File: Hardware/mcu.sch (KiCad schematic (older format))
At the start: 10 parts, among them SW3 SW_PUSH, U1 STM32F411RE_LQFP64

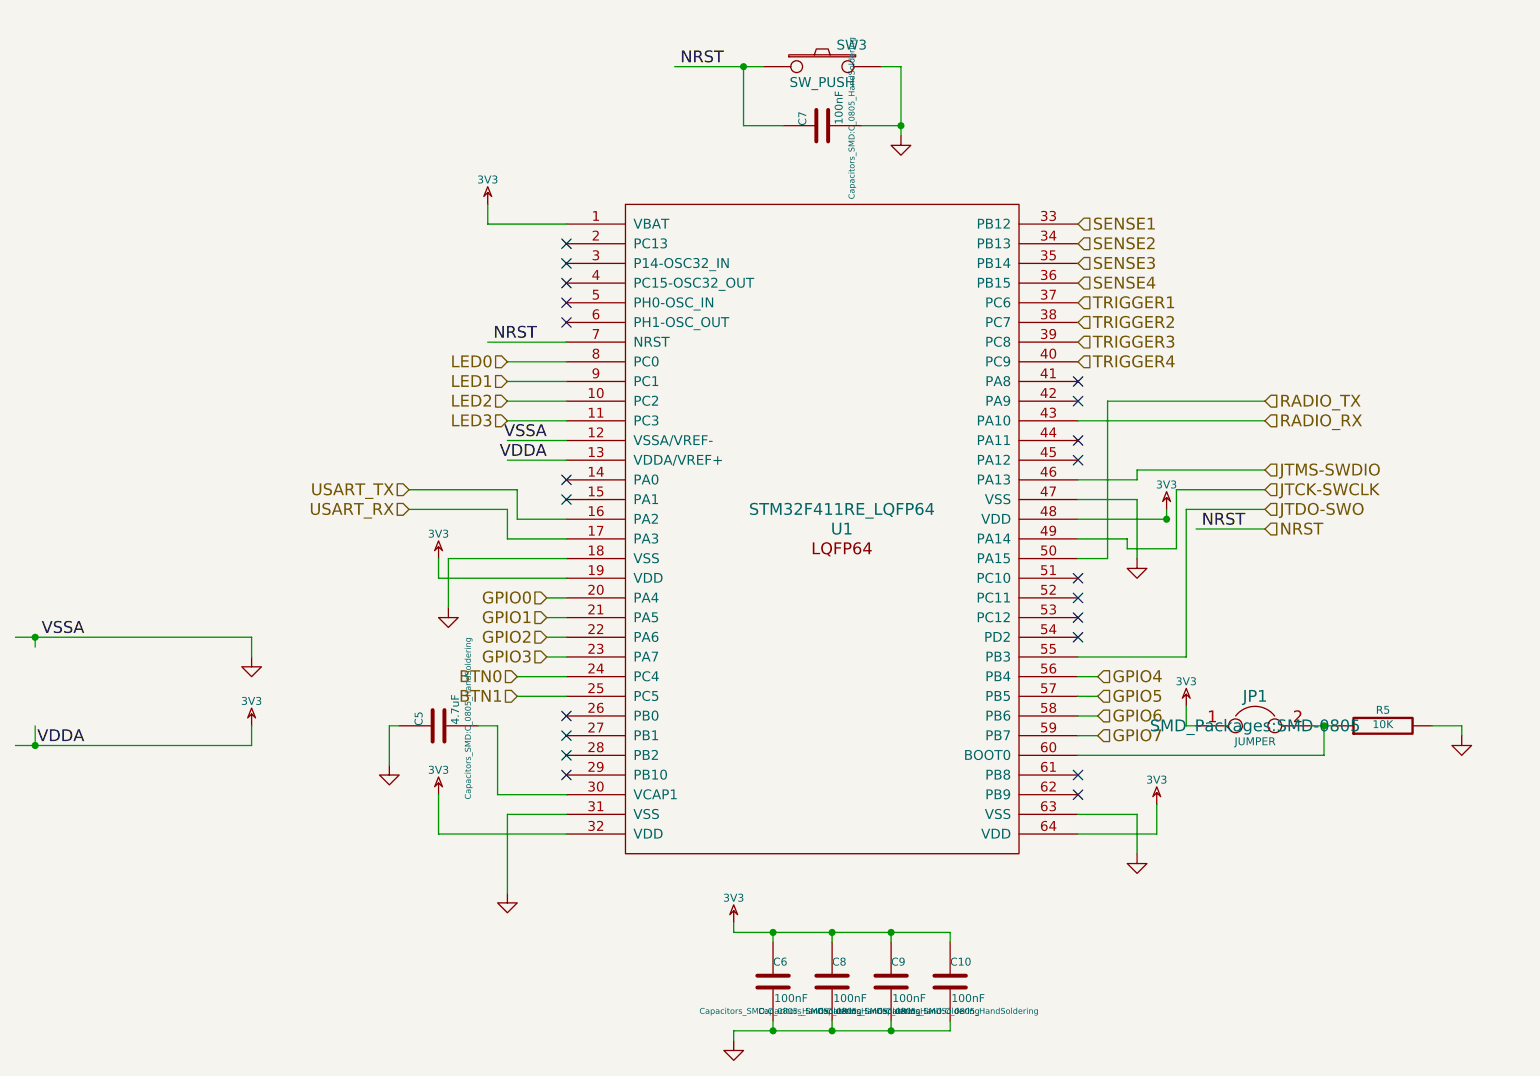
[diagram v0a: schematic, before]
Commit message: Added sensors and sensor passives
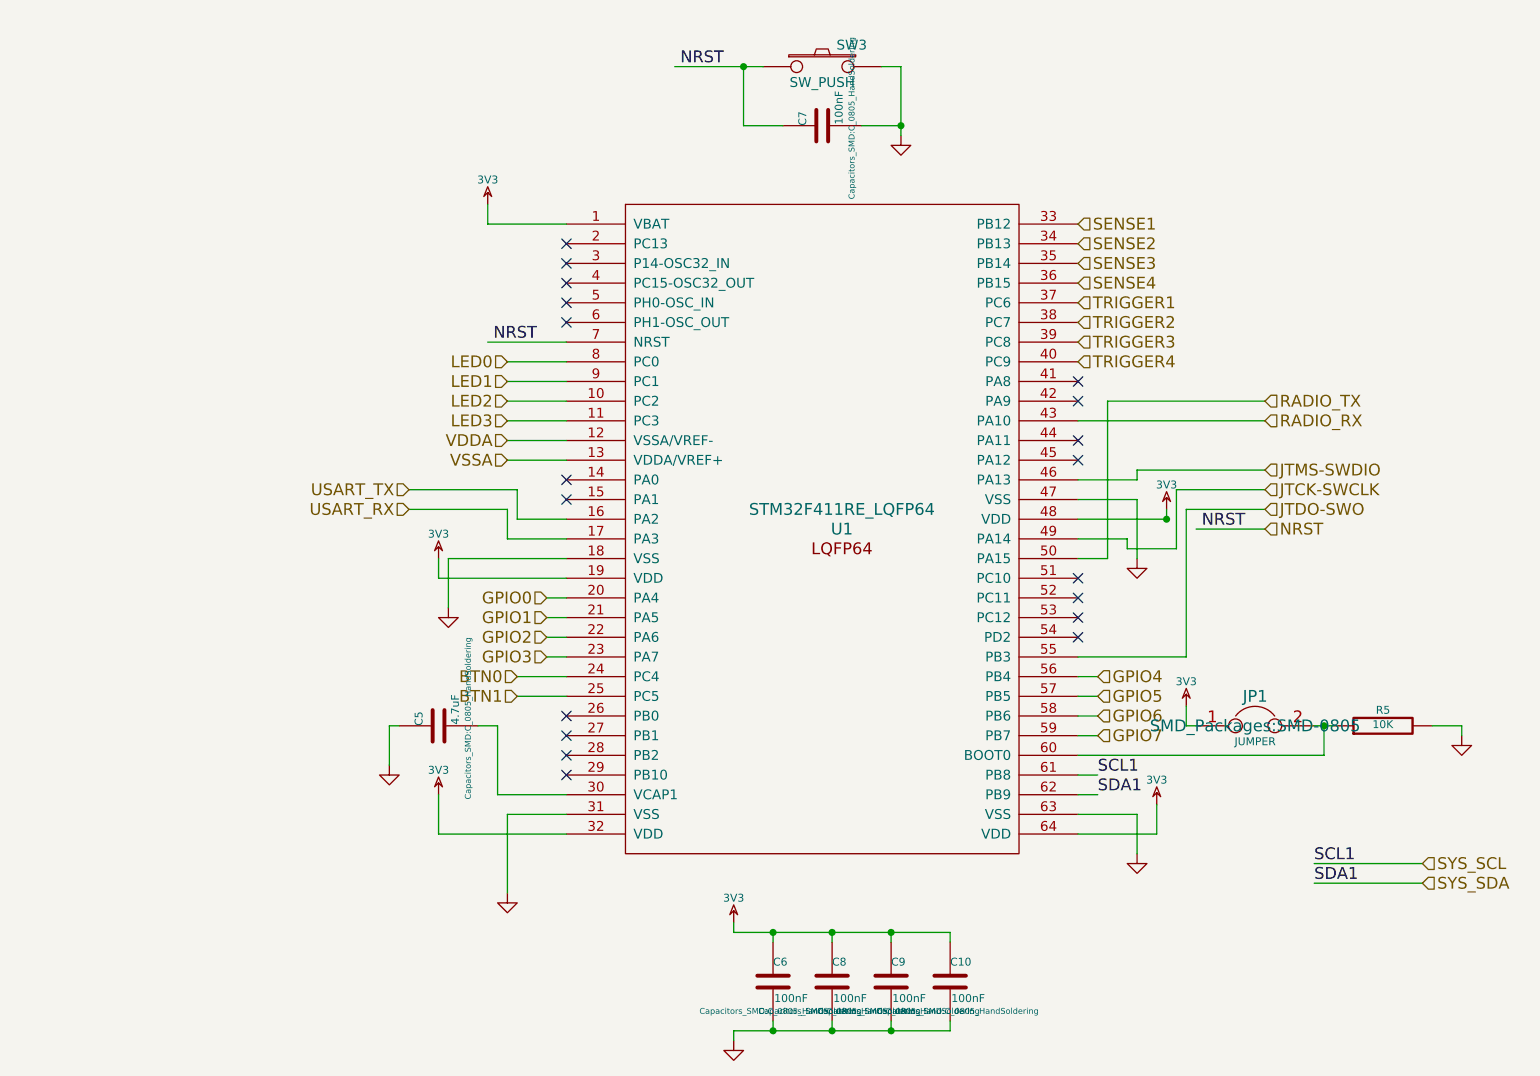
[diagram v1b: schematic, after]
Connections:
- net labels added: SCL1, SDA1, SYS_SCL, SYS_SDA
- wire segments 93 -> 91
- no-connect marks 21 -> 19
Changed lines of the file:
@@
 LIBS:STM32-Additional
 LIBS:xbee
+LIBS:Passives
 LIBS:avbay-cache
-EELAYER 27 0
+EELAYER 25 0
 EELAYER END
 $Descr USLetter 11000 8500
 encoding utf-8
-Sheet 2 4
+Sheet 4 5
 Title "MCU"
 Date "6 dec 2014"
@@
 $EndDescr
 $Comp
-L 3V3 #PWR12
+L 3V3 #PWR018
 U 1 1 542CDA8F
 P 3800 3600
-F 0 "#PWR12" H 3800 3700 40  0001 C CNN
+F 0 "#PWR018" H 3800 3700 40  0001 C CNN
 F 1 "3V3" H 3800 3725 40  0000 C CNN
 F 2 "" H 3800 3600 60  0000 C CNN
@@
 $EndComp
 $Comp
-L GND #PWR14
+L GND #PWR019
 U 1 1 542CDA9E
 P 3850 3850
-F 0 "#PWR14" H 3850 3850 30  0001 C CNN
+F 0 "#PWR019" H 3850 3850 30  0001 C CNN
 F 1 "GND" H 3850 3780 30  0001 C CNN
 F 2 "" H 3850 3850 60  0000 C CNN
@@
 $EndComp
 $Comp
-L 3V3 #PWR13
+L 3V3 #PWR020
 U 1 1 542CDAB1
 P 3800 4800
-F 0 "#PWR13" H 3800 4900 40  0001 C CNN
+F 0 "#PWR020" H 3800 4900 40  0001 C CNN
 F 1 "3V3" H 3800 4925 40  0000 C CNN
 F 2 "" H 3800 4800 60  0000 C CNN
@@
 $EndComp
 $Comp
-L 3V3 #PWR22
+L 3V3 #PWR021
 U 1 1 542CDAB7
 P 7450 4850
-F 0 "#PWR22" H 7450 4950 40  0001 C CNN
+F 0 "#PWR021" H 7450 4950 40  0001 C CNN
 F 1 "3V3" H 7450 4975 40  0000 C CNN
 F 2 "" H 7450 4850 60  0000 C CNN
@@
 $EndComp
 $Comp
-L 3V3 #PWR23
+L 3V3 #PWR022
 U 1 1 542CDC4D
 P 7500 3350
-F 0 "#PWR23" H 7500 3450 40  0001 C CNN
+F 0 "#PWR022" H 7500 3450 40  0001 C CNN
 F 1 "3V3" H 7500 3475 40  0000 C CNN
 F 2 "" H 7500 3350 60  0000 C CNN
@@
 $EndComp
 $Comp
-L GND #PWR19
+L GND #PWR023
 U 1 1 5430D873
 P 6150 1450
-F 0 "#PWR19" H 6150 1450 30  0001 C CNN
+F 0 "#PWR023" H 6150 1450 30  0001 C CNN
 F 1 "GND" H 6150 1380 30  0001 C CNN
 F 2 "" H 6150 1450 60  0000 C CNN
@@
 $EndComp
 $Comp
-L 3V3 #PWR24
+L 3V3 #PWR024
 U 1 1 5430DC01
 P 7600 4350
-F 0 "#PWR24" H 7600 4450 40  0001 C CNN
+F 0 "#PWR024" H 7600 4450 40  0001 C CNN
 F 1 "3V3" H 7600 4475 40  0000 C CNN
 F 2 "" H 7600 4350 60  0000 C CNN
@@
 $EndComp
 $Comp
-L GND #PWR25
+L GND #PWR025
 U 1 1 5430DC07
 P 9000 4500
-F 0 "#PWR25" H 9000 4500 30  0001 C CNN
+F 0 "#PWR025" H 9000 4500 30  0001 C CNN
 F 1 "GND" H 9000 4430 30  0001 C CNN
 F 2 "" H 9000 4500 60  0000 C CNN
@@
 $EndComp
 $Comp
-L 3V3 #PWR17
+L 3V3 #PWR026
 U 1 1 5430E0CC
 P 5300 5450
-F 0 "#PWR17" H 5300 5550 40  0001 C CNN
+F 0 "#PWR026" H 5300 5550 40  0001 C CNN
 F 1 "3V3" H 5300 5575 40  0000 C CNN
 F 2 "" H 5300 5450 60  0000 C CNN
@@
 $EndComp
 $Comp
-L GND #PWR18
+L GND #PWR027
 U 1 1 5430E365
 P 5300 6050
-F 0 "#PWR18" H 5300 6050 30  0001 C CNN
+F 0 "#PWR027" H 5300 6050 30  0001 C CNN
 F 1 "GND" H 5300 5980 30  0001 C CNN
 F 2 "" H 5300 6050 60  0000 C CNN
@@
 $EndComp
 $Comp
-L GND #PWR11
+L GND #PWR028
 U 1 1 5430E5BA
 P 3550 4650
-F 0 "#PWR11" H 3550 4650 30  0001 C CNN
+F 0 "#PWR028" H 3550 4650 30  0001 C CNN
 F 1 "GND" H 3550 4580 30  0001 C CNN
 F 2 "" H 3550 4650 60  0000 C CNN
@@
 Text HLabel 8000 2900 2    60   Input ~ 0
 RADIO_RX
-Text Label 4350 3100 2    60   ~ 0
-VDDA
-Text Label 4350 3000 2    60   ~ 0
-VSSA
-Text Label 2000 4000 2    60   ~ 0
-VSSA
-Text Label 2000 4550 2    60   ~ 0
-VDDA
-$Comp
-L 3V3 #PWR15
+$Comp
+L 3V3 #PWR029
 U 1 1 5430E17B
 P 4050 1800
-F 0 "#PWR15" H 4050 1900 40  0001 C CNN
+F 0 "#PWR029" H 4050 1900 40  0001 C CNN
 F 1 "3V3" H 4050 1925 40  0000 C CNN
 F 2 "" H 4050 1800 60  0000 C CNN
 F 3 "" H 4050 1800 60  0000 C CNN
 	1    4050 1800
-	1    0    0    -1
-$EndComp
-$Comp
-L GND #PWR9
-U 1 1 5430E3DA
-P 2850 4100
-F 0 "#PWR9" H 2850 4100 30  0001 C CNN
-F 1 "GND" H 2850 4030 30  0001 C CNN
-F 2 "" H 2850 4100 60  0000 C CNN
-F 3 "" H 2850 4100 60  0000 C CNN
-	1    2850 4100
-	1    0    0    -1
-$EndComp
-$Comp
-L 3V3 #PWR10
-U 1 1 5430E3E0
-P 2850 4450
-F 0 "#PWR10" H 2850 4550 40  0001 C CNN
-F 1 "3V3" H 2850 4575 40  0000 C CNN
-F 2 "" H 2850 4450 60  0000 C CNN
-F 3 "" H 2850 4450 60  0000 C CNN
-	1    2850 4450
 	1    0    0    -1
 $EndComp
@@
 	7200 2800 8000 2800
 Wire Wire Line
-	1650 4000 2850 4000
-Wire Wire Line
-	1650 4550 2850 4550
-Wire Wire Line
 	4050 1900 4450 1900
 Wire Wire Line
 	4050 1800 4050 1900
-Wire Wire Line
-	2850 4000 2850 4100
-Wire Wire Line
-	2850 4550 2850 4450
-Wire Wire Line
-	1750 4450 1750 4550
-Connection ~ 1750 4550
-Wire Wire Line
-	1750 4050 1750 4000
-Connection ~ 1750 4000
 Wire Wire Line
 	8000 2900 7050 2900
@@
 NoConn ~ 7050 3900
 NoConn ~ 7050 4000
-NoConn ~ 7050 4700
-NoConn ~ 7050 4800
 NoConn ~ 4450 4700
 NoConn ~ 4450 4600
@@
 	4150 4900 4150 5300
 $Comp
-L GND #PWR16
+L GND #PWR030
 U 1 1 54449600
 P 4150 5300
-F 0 "#PWR16" H 4150 5300 30  0001 C CNN
+F 0 "#PWR030" H 4150 5300 30  0001 C CNN
 F 1 "GND" H 4150 5230 30  0001 C CNN
 F 2 "" H 4150 5300 60  0000 C CNN
@@
 	7350 4900 7350 5100
 $Comp
-L GND #PWR20
+L GND #PWR031
 U 1 1 5444A762
 P 7350 3600
-F 0 "#PWR20" H 7350 3600 30  0001 C CNN
+F 0 "#PWR031" H 7350 3600 30  0001 C CNN
 F 1 "GND" H 7350 3530 30  0001 C CNN
 F 2 "" H 7350 3600 60  0000 C CNN
@@
 	7350 3300 7350 3600
 $Comp
-L GND #PWR21
+L GND #PWR032
 U 1 1 54449656
 P 7350 5100
-F 0 "#PWR21" H 7350 5100 30  0001 C CNN
+F 0 "#PWR032" H 7350 5100 30  0001 C CNN
 F 1 "GND" H 7350 5030 30  0001 C CNN
 F 2 "" H 7350 5100 60  0000 C CNN
@@
 NoConn ~ 4450 2300
 NoConn ~ 4450 2400
+Wire Wire Line
+	7050 4700 7150 4700
+Wire Wire Line
+	7050 4800 7150 4800
+Text Label 7150 4700 0    60   ~ 0
+SCL1
+Text Label 7150 4800 0    60   ~ 0
+SDA1
+Wire Wire Line
+	8250 5150 8800 5150
+Wire Wire Line
+	8250 5250 8800 5250
+Text Label 8250 5150 0    60   ~ 0
+SCL1
+Text Label 8250 5250 0    60   ~ 0
+SDA1
+Text HLabel 8800 5150 2    60   Input ~ 0
+SYS_SCL
+Text HLabel 8800 5250 2    60   Input ~ 0
+SYS_SDA
+Text HLabel 4150 3000 0    60   Input ~ 0
+VDDA
+Text HLabel 4150 3100 0    60   Input ~ 0
+VSSA
 $EndSCHEMATC

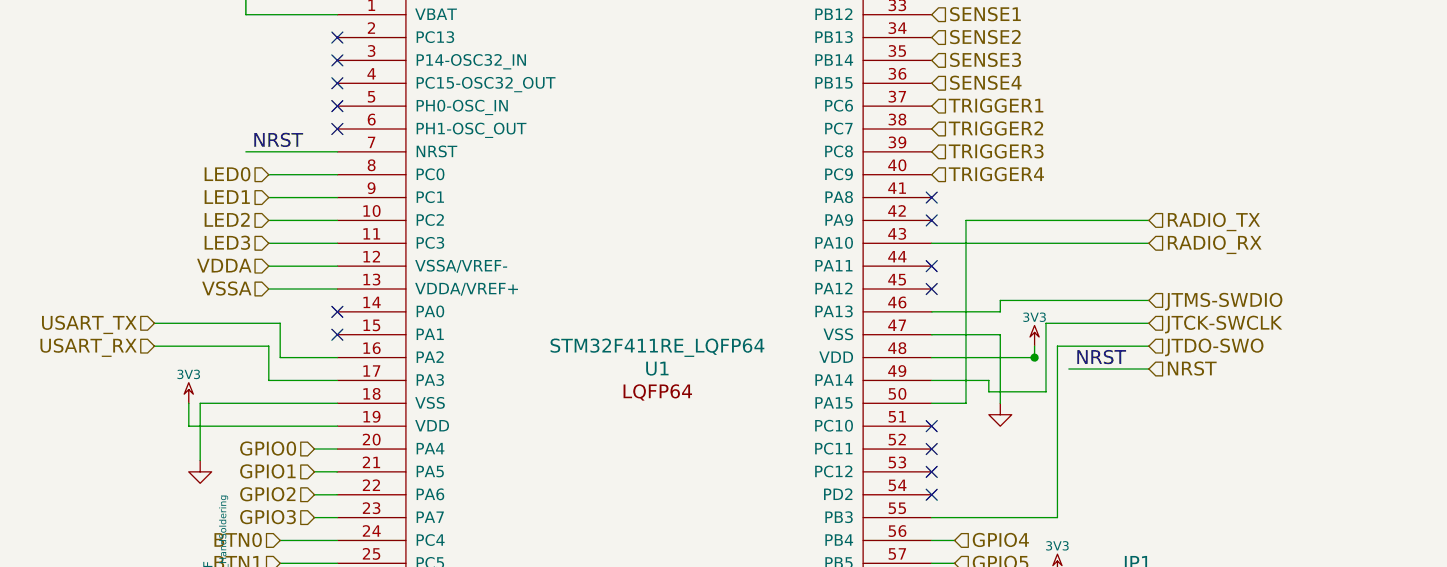
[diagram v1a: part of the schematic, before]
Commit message: Roughed out PCB layout
Known issues:
- SW_PUSH holes too small. New footprint needed
- Sensor footprints are completely wrong.
- Regulator footprints might not be correct.

Tasks:
- Place passives according to schematic (especially
  with decoupling capacitors.
- Condense layout as much as possible for
  smallest board size
- Route board
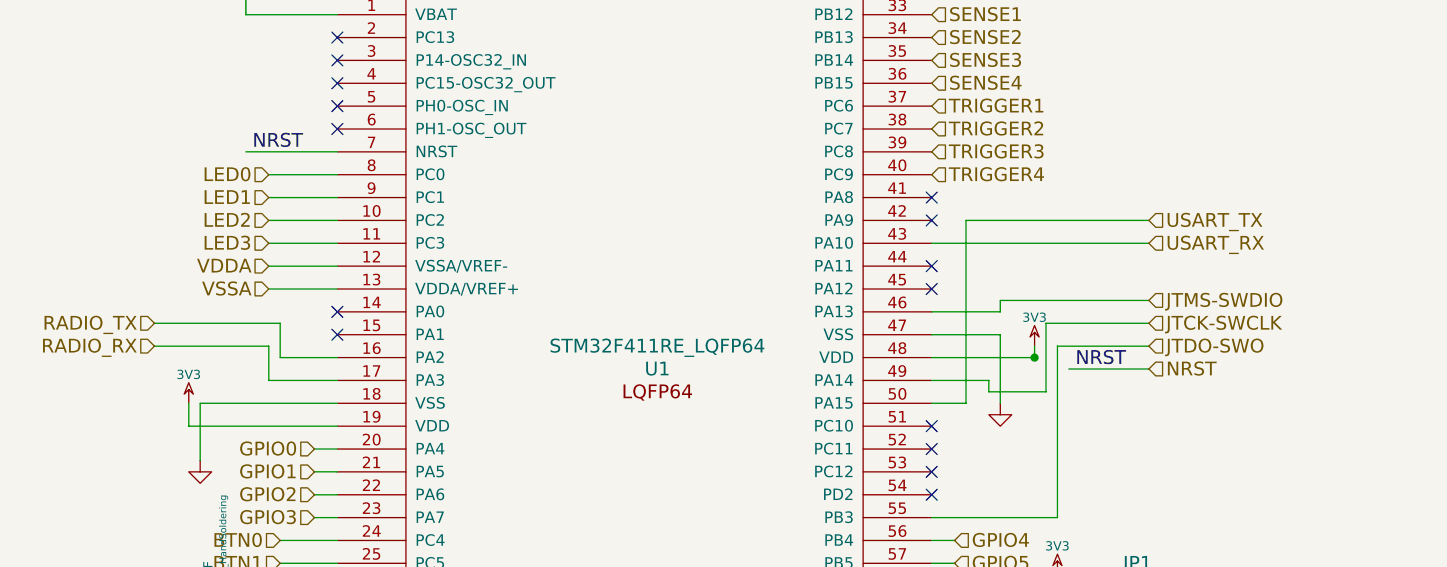
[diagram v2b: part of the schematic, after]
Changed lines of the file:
@@
 $EndDescr
 $Comp
-L 3V3 #PWR018
+L 3V3 #PWR021
 U 1 1 542CDA8F
 P 3800 3600
-F 0 "#PWR018" H 3800 3700 40  0001 C CNN
+F 0 "#PWR021" H 3800 3700 40  0001 C CNN
 F 1 "3V3" H 3800 3725 40  0000 C CNN
 F 2 "" H 3800 3600 60  0000 C CNN
@@
 $EndComp
 $Comp
-L GND #PWR019
+L GND #PWR022
 U 1 1 542CDA9E
 P 3850 3850
-F 0 "#PWR019" H 3850 3850 30  0001 C CNN
+F 0 "#PWR022" H 3850 3850 30  0001 C CNN
 F 1 "GND" H 3850 3780 30  0001 C CNN
 F 2 "" H 3850 3850 60  0000 C CNN
@@
 $EndComp
 $Comp
-L 3V3 #PWR020
+L 3V3 #PWR023
 U 1 1 542CDAB1
 P 3800 4800
-F 0 "#PWR020" H 3800 4900 40  0001 C CNN
+F 0 "#PWR023" H 3800 4900 40  0001 C CNN
 F 1 "3V3" H 3800 4925 40  0000 C CNN
 F 2 "" H 3800 4800 60  0000 C CNN
@@
 $EndComp
 $Comp
-L 3V3 #PWR021
+L 3V3 #PWR024
 U 1 1 542CDAB7
 P 7450 4850
-F 0 "#PWR021" H 7450 4950 40  0001 C CNN
+F 0 "#PWR024" H 7450 4950 40  0001 C CNN
 F 1 "3V3" H 7450 4975 40  0000 C CNN
 F 2 "" H 7450 4850 60  0000 C CNN
@@
 $EndComp
 $Comp
-L 3V3 #PWR022
+L 3V3 #PWR025
 U 1 1 542CDC4D
 P 7500 3350
-F 0 "#PWR022" H 7500 3450 40  0001 C CNN
+F 0 "#PWR025" H 7500 3450 40  0001 C CNN
 F 1 "3V3" H 7500 3475 40  0000 C CNN
 F 2 "" H 7500 3350 60  0000 C CNN
@@
 NRST
 Text HLabel 3650 3250 0    60   Input ~ 0
-USART_TX
+RADIO_TX
 Text HLabel 3650 3350 0    60   Input ~ 0
-USART_RX
+RADIO_RX
 Text Label 5250 1100 2    60   ~ 0
 NRST
@@
 $EndComp
 $Comp
-L GND #PWR023
+L GND #PWR026
 U 1 1 5430D873
 P 6150 1450
-F 0 "#PWR023" H 6150 1450 30  0001 C CNN
+F 0 "#PWR026" H 6150 1450 30  0001 C CNN
 F 1 "GND" H 6150 1380 30  0001 C CNN
 F 2 "" H 6150 1450 60  0000 C CNN
@@
 $EndComp
 $Comp
-L 3V3 #PWR024
+L 3V3 #PWR027
 U 1 1 5430DC01
 P 7600 4350
-F 0 "#PWR024" H 7600 4450 40  0001 C CNN
+F 0 "#PWR027" H 7600 4450 40  0001 C CNN
 F 1 "3V3" H 7600 4475 40  0000 C CNN
 F 2 "" H 7600 4350 60  0000 C CNN
@@
 $EndComp
 $Comp
-L GND #PWR025
+L GND #PWR028
 U 1 1 5430DC07
 P 9000 4500
-F 0 "#PWR025" H 9000 4500 30  0001 C CNN
+F 0 "#PWR028" H 9000 4500 30  0001 C CNN
 F 1 "GND" H 9000 4430 30  0001 C CNN
 F 2 "" H 9000 4500 60  0000 C CNN
@@
 $EndComp
 $Comp
-L 3V3 #PWR026
+L 3V3 #PWR029
 U 1 1 5430E0CC
 P 5300 5450
-F 0 "#PWR026" H 5300 5550 40  0001 C CNN
+F 0 "#PWR029" H 5300 5550 40  0001 C CNN
 F 1 "3V3" H 5300 5575 40  0000 C CNN
 F 2 "" H 5300 5450 60  0000 C CNN
@@
 $EndComp
 $Comp
-L GND #PWR027
+L GND #PWR030
 U 1 1 5430E365
 P 5300 6050
-F 0 "#PWR027" H 5300 6050 30  0001 C CNN
+F 0 "#PWR030" H 5300 6050 30  0001 C CNN
 F 1 "GND" H 5300 5980 30  0001 C CNN
 F 2 "" H 5300 6050 60  0000 C CNN
@@
 $EndComp
 $Comp
-L GND #PWR028
+L GND #PWR031
 U 1 1 5430E5BA
 P 3550 4650
-F 0 "#PWR028" H 3550 4650 30  0001 C CNN
+F 0 "#PWR031" H 3550 4650 30  0001 C CNN
 F 1 "GND" H 3550 4580 30  0001 C CNN
 F 2 "" H 3550 4650 60  0000 C CNN
@@
 $EndComp
 Text HLabel 8000 2800 2    60   Input ~ 0
-RADIO_TX
+USART_TX
 Text HLabel 8000 2900 2    60   Input ~ 0
-RADIO_RX
-$Comp
-L 3V3 #PWR029
+USART_RX
+$Comp
+L 3V3 #PWR032
 U 1 1 5430E17B
 P 4050 1800
-F 0 "#PWR029" H 4050 1900 40  0001 C CNN
+F 0 "#PWR032" H 4050 1900 40  0001 C CNN
 F 1 "3V3" H 4050 1925 40  0000 C CNN
 F 2 "" H 4050 1800 60  0000 C CNN
@@
 	4150 4900 4150 5300
 $Comp
-L GND #PWR030
+L GND #PWR033
 U 1 1 54449600
 P 4150 5300
-F 0 "#PWR030" H 4150 5300 30  0001 C CNN
+F 0 "#PWR033" H 4150 5300 30  0001 C CNN
 F 1 "GND" H 4150 5230 30  0001 C CNN
 F 2 "" H 4150 5300 60  0000 C CNN
@@
 	7350 4900 7350 5100
 $Comp
-L GND #PWR031
+L GND #PWR034
 U 1 1 5444A762
 P 7350 3600
-F 0 "#PWR031" H 7350 3600 30  0001 C CNN
+F 0 "#PWR034" H 7350 3600 30  0001 C CNN
 F 1 "GND" H 7350 3530 30  0001 C CNN
 F 2 "" H 7350 3600 60  0000 C CNN
@@
 	7350 3300 7350 3600
 $Comp
-L GND #PWR032
+L GND #PWR035
 U 1 1 54449656
 P 7350 5100
-F 0 "#PWR032" H 7350 5100 30  0001 C CNN
+F 0 "#PWR035" H 7350 5100 30  0001 C CNN
 F 1 "GND" H 7350 5030 30  0001 C CNN
 F 2 "" H 7350 5100 60  0000 C CNN
